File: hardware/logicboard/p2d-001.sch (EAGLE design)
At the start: 55 parts, among them IC1 74LS06N, IC2 4066N, J1 MKR, J2 GPIO, J3 Vcc, J4 RLY, J5 SPI, J7 DIN5, J8 DIN5, J9 DIN5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

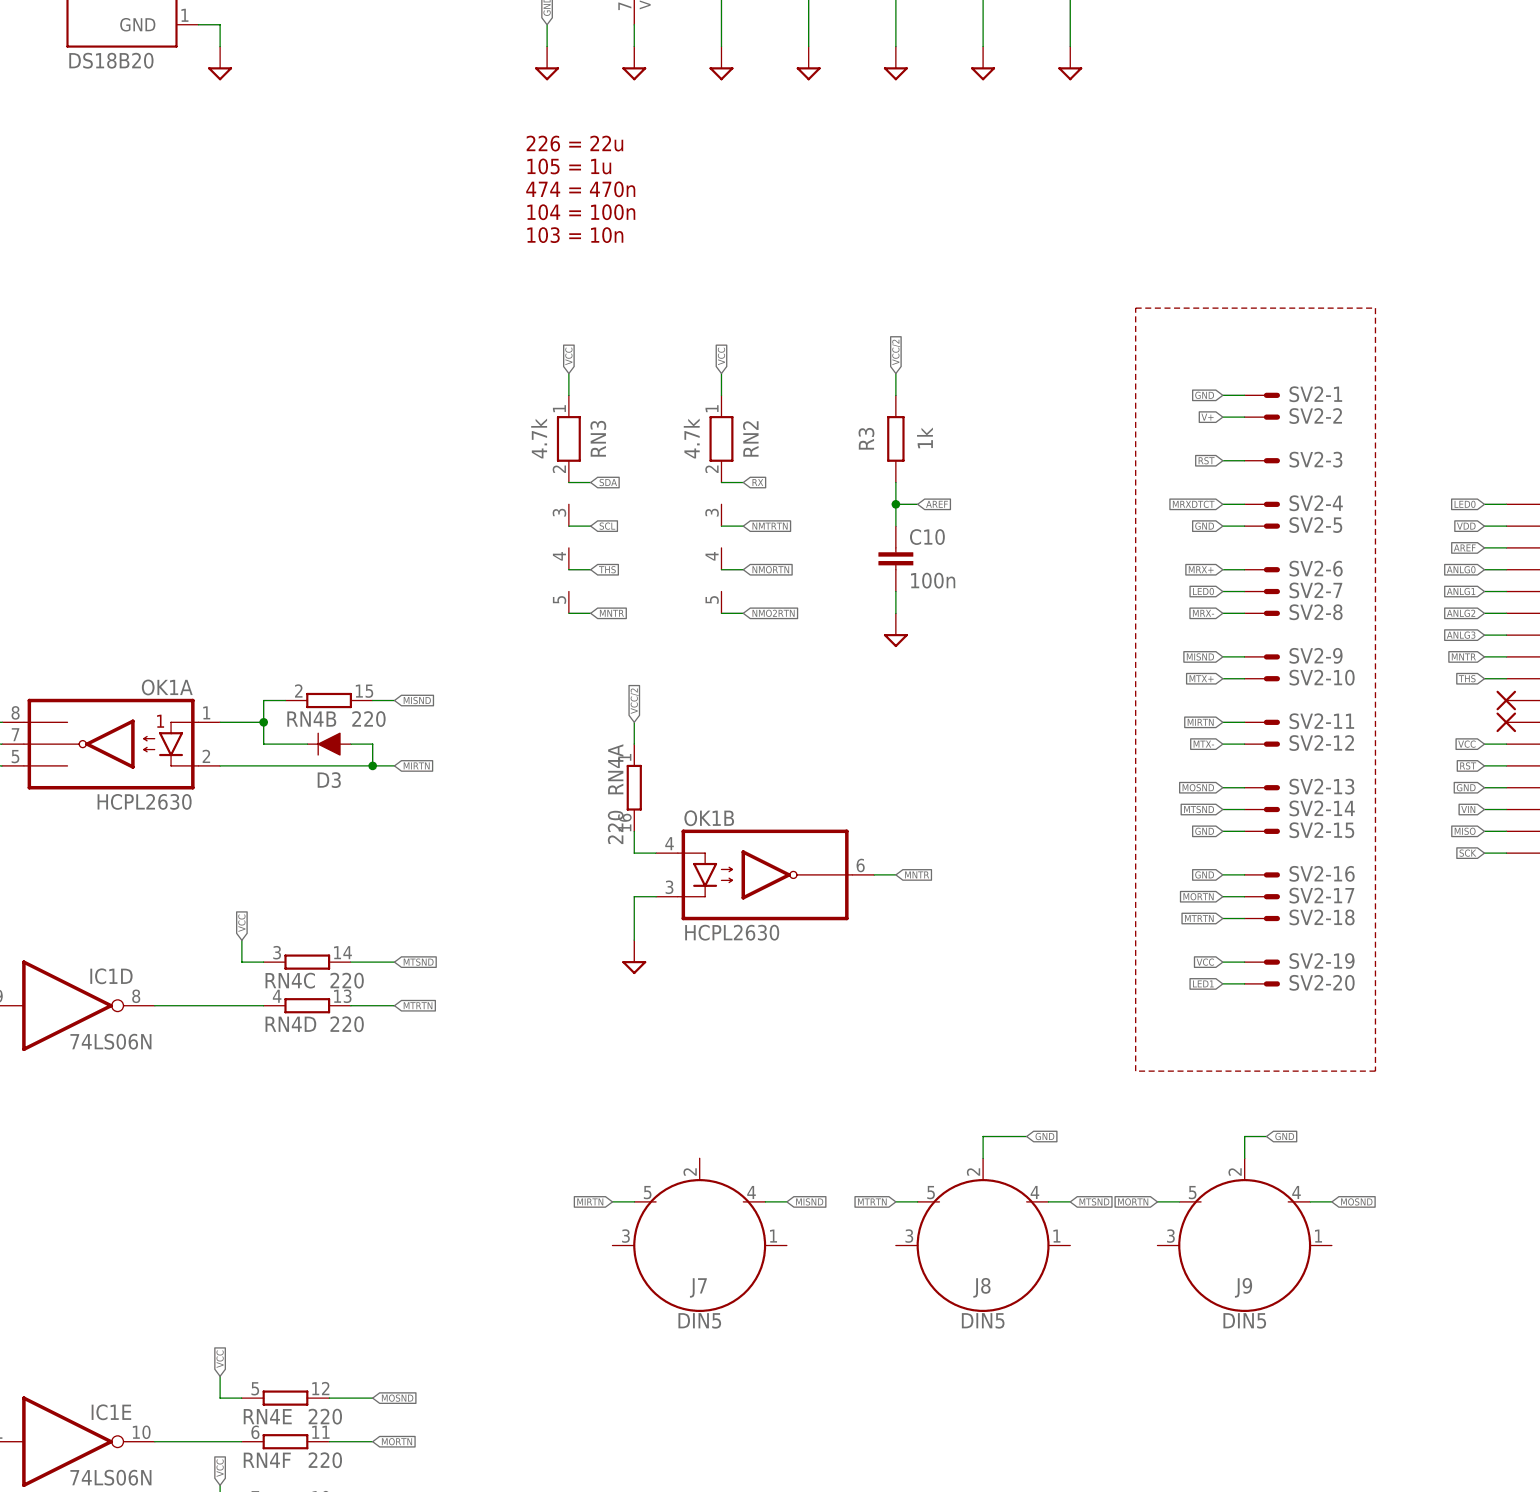
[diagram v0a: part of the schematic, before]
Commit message: Changed dimension of the board.
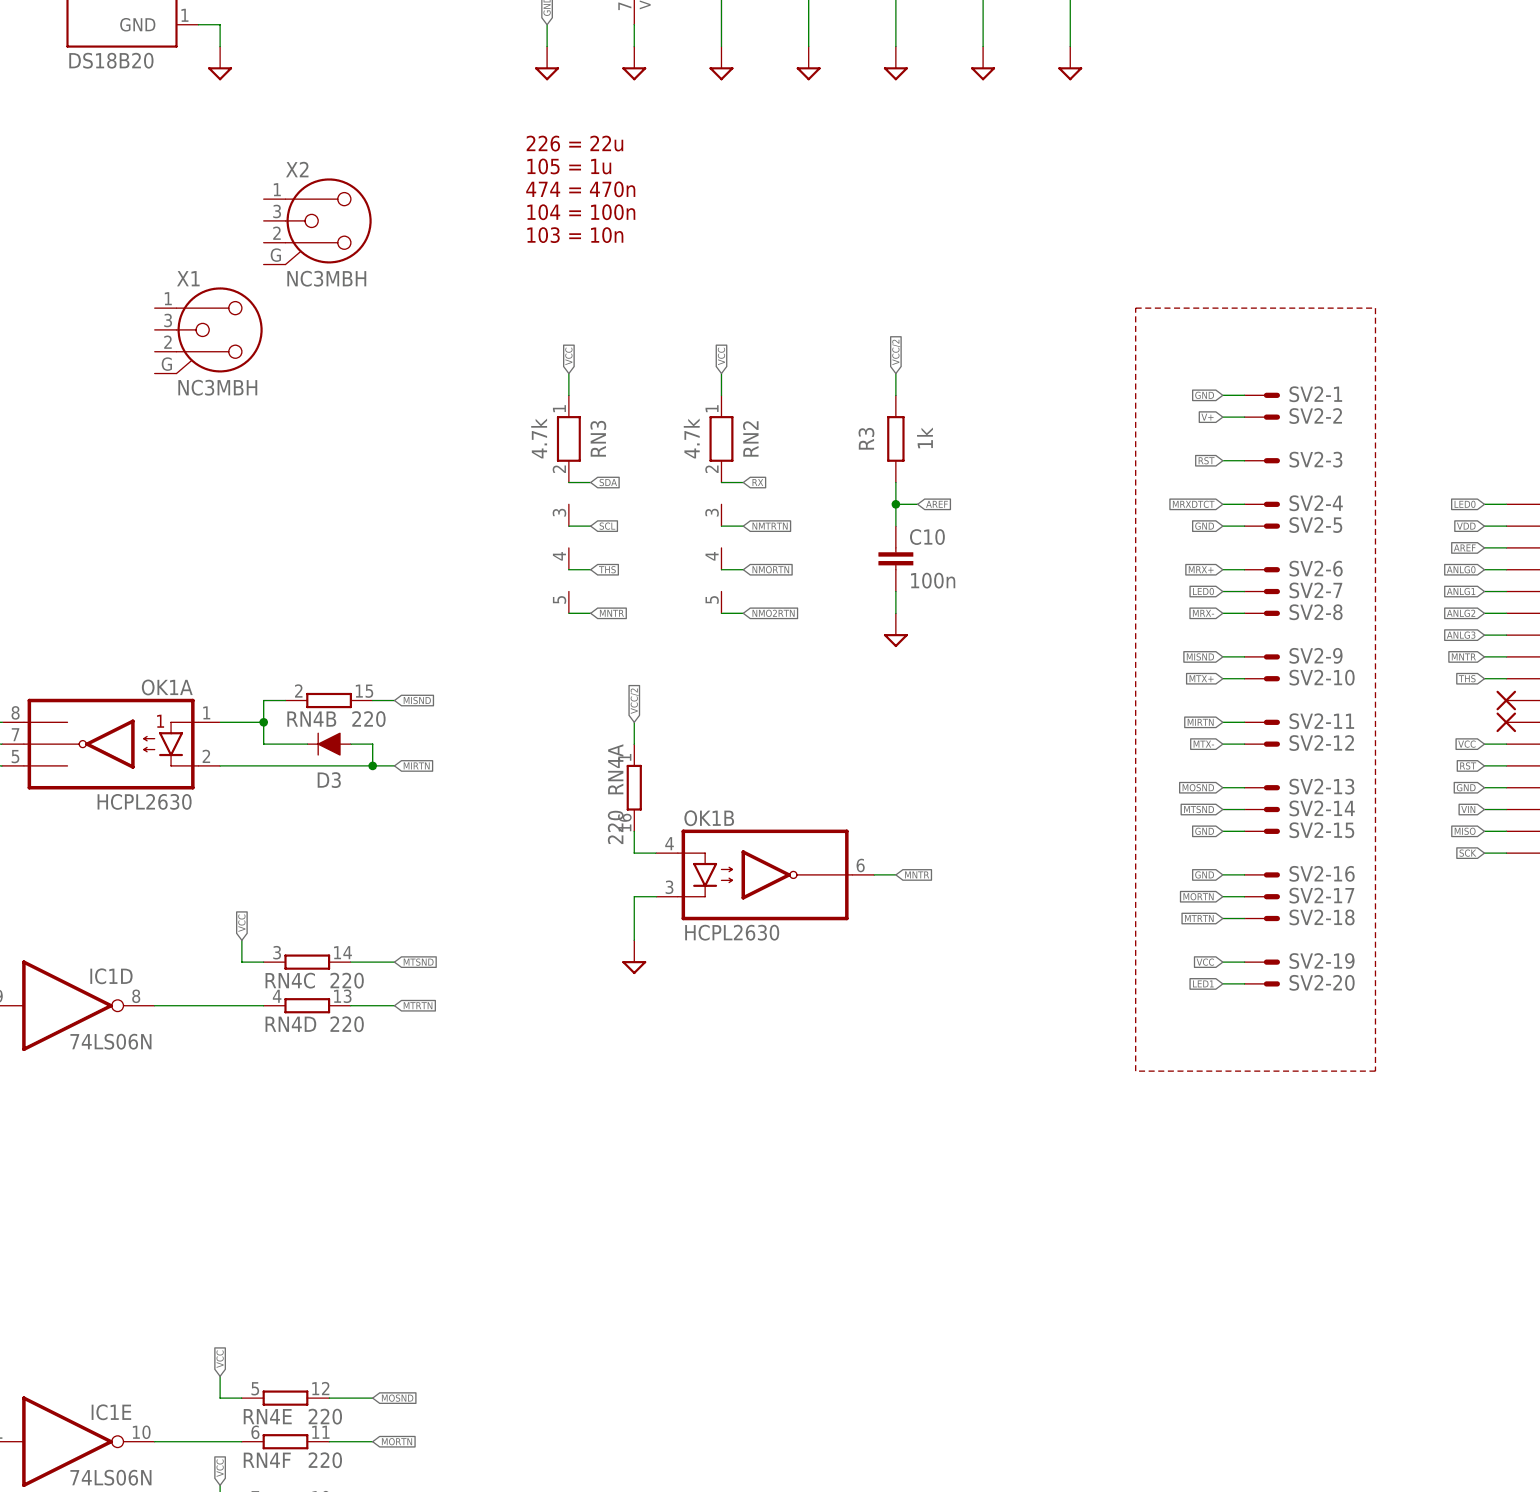
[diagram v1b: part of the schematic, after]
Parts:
- removed J7, J8, J9: DIN5, SparkFun-Connectors:DIN5
- added X1, X2: NC3MBH, con-neutrik_ag:NC3MBH
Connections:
- net GND: no longer J8.2, J9.2
- net MIRTN: no longer J7.5
- net MISND: no longer J7.4
- net MORTN: no longer J9.5
- net MOSND: no longer J9.4
- net MTRTN: no longer J8.5
- net MTSND: no longer J8.4
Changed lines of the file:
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@@
 <part name="V+" library="wirepad" library_urn="urn:adsk.eagle:library:412" deviceset="SMD2" device="" package3d_urn="urn:adsk.eagle:package:30839/1"/>
 <part name="VIN" library="wirepad" library_urn="urn:adsk.eagle:library:412" deviceset="SMD2" device="" package3d_urn="urn:adsk.eagle:package:30839/1"/>
-<part name="J7" library="SparkFun-Connectors" library_urn="urn:adsk.eagle:library:513" deviceset="DIN5" device="" package3d_urn="urn:adsk.eagle:package:38294/1"/>
-<part name="J8" library="SparkFun-Connectors" library_urn="urn:adsk.eagle:library:513" deviceset="DIN5" device="" package3d_urn="urn:adsk.eagle:package:38294/1"/>
-<part name="J9" library="SparkFun-Connectors" library_urn="urn:adsk.eagle:library:513" deviceset="DIN5" device="" package3d_urn="urn:adsk.eagle:package:38294/1"/>
 <part name="J0" library="con-jack" library_urn="urn:adsk.eagle:library:154" deviceset="JACK-PLUG" device="0" package3d_urn="urn:adsk.eagle:package:7492/1"/>
 <part name="R4" library="resistor" library_urn="urn:adsk.eagle:library:348" deviceset="R-EU_" device="0204/5" package3d_urn="urn:adsk.eagle:package:23488/1" value="1k"/>
@@
 <part name="SV3" library="con-ml" library_urn="urn:adsk.eagle:library:164" deviceset="ML14E" device="" package3d_urn="urn:adsk.eagle:package:8693/1"/>
 <part name="J6" library="SparkFun-Connectors" library_urn="urn:adsk.eagle:library:513" deviceset="CONN_03" device="JST-PTH-VERT" package3d_urn="urn:adsk.eagle:package:38080/1"/>
+<part name="X1" library="con-neutrik_ag" library_urn="urn:adsk.eagle:library:166" deviceset="NC3" device="MBH" package3d_urn="urn:adsk.eagle:package:8841/1"/>
+<part name="X2" library="con-neutrik_ag" library_urn="urn:adsk.eagle:library:166" deviceset="NC3" device="MBH" package3d_urn="urn:adsk.eagle:package:8841/1"/>
 </parts>
 <sheets>
@@
 <attribute name="VALUE" x="90.678" y="242.443" size="1.778" layer="96" rot="R270"/>
 </instance>
-<instance part="J7" gate="G$1" x="248.92" y="60.96" smashed="yes">
-<attribute name="NAME" x="248.92" y="55.372" size="1.778" layer="95" font="vector" align="bottom-center"/>
-<attribute name="VALUE" x="248.92" y="53.086" size="1.778" layer="96" font="vector" align="top-center"/>
-</instance>
-<instance part="J8" gate="G$1" x="281.94" y="60.96" smashed="yes">
-<attribute name="NAME" x="281.94" y="55.372" size="1.778" layer="95" font="vector" align="bottom-center"/>
-<attribute name="VALUE" x="281.94" y="53.086" size="1.778" layer="96" font="vector" align="top-center"/>
-</instance>
-<instance part="J9" gate="G$1" x="312.42" y="60.96" smashed="yes">
-<attribute name="NAME" x="312.42" y="55.372" size="1.778" layer="95" font="vector" align="bottom-center"/>
-<attribute name="VALUE" x="312.42" y="53.086" size="1.778" layer="96" font="vector" align="top-center"/>
-</instance>
 <instance part="J0" gate="G$1" x="33.02" y="198.12" smashed="yes">
 <attribute name="NAME" x="25.4" y="203.2" size="1.778" layer="95"/>
@@
 <attribute name="VALUE" x="63.5" y="12.954" size="1.778" layer="96" font="vector"/>
 <attribute name="NAME" x="63.5" y="25.908" size="1.778" layer="95" font="vector"/>
+</instance>
+<instance part="X1" gate="G$1" x="193.04" y="167.64" smashed="yes">
+<attribute name="NAME" x="187.96" y="172.72" size="1.778" layer="95"/>
+<attribute name="VALUE" x="187.96" y="160.02" size="1.778" layer="96"/>
+</instance>
+<instance part="X2" gate="G$1" x="205.74" y="180.34" smashed="yes">
+<attribute name="NAME" x="200.66" y="185.42" size="1.778" layer="95"/>
+<attribute name="VALUE" x="200.66" y="172.72" size="1.778" layer="96"/>
 </instance>
 </instances>
@@
 </segment>
 <segment>
-<pinref part="J8" gate="G$1" pin="2"/>
-<wire x1="281.94" y1="71.12" x2="281.94" y2="73.66" width="0.1524" layer="91"/>
-<wire x1="281.94" y1="73.66" x2="287.02" y2="73.66" width="0.1524" layer="91"/>
-<label x="287.02" y="73.66" size="0.8128" layer="95" xref="yes"/>
-</segment>
-<segment>
-<pinref part="J9" gate="G$1" pin="2"/>
-<wire x1="312.42" y1="71.12" x2="312.42" y2="73.66" width="0.1524" layer="91"/>
-<wire x1="312.42" y1="73.66" x2="314.96" y2="73.66" width="0.1524" layer="91"/>
-<label x="314.96" y="73.66" size="0.8128" layer="95" xref="yes"/>
-</segment>
-<segment>
 <pinref part="SUPPLY2" gate="GND" pin="GND"/>
 <wire x1="271.78" y1="208.28" x2="271.78" y2="200.66" width="0.1524" layer="91"/>
@@
 </segment>
 <segment>
-<pinref part="J7" gate="G$1" pin="4"/>
-<wire x1="256.54" y1="66.04" x2="259.08" y2="66.04" width="0.1524" layer="91"/>
-<label x="259.08" y="66.04" size="0.8128" layer="95" xref="yes"/>
-</segment>
-<segment>
 <pinref part="SV2" gate="-9" pin="S"/>
 <wire x1="312.42" y1="129.54" x2="309.88" y2="129.54" width="0.1524" layer="91"/>
@@
 </segment>
 <segment>
-<pinref part="J7" gate="G$1" pin="5"/>
-<wire x1="241.3" y1="66.04" x2="238.76" y2="66.04" width="0.1524" layer="91"/>
-<label x="238.76" y="66.04" size="0.8128" layer="95" rot="R180" xref="yes"/>
-</segment>
-<segment>
 <pinref part="SV2" gate="-11" pin="S"/>
 <wire x1="312.42" y1="121.92" x2="309.88" y2="121.92" width="0.1524" layer="91"/>
@@
 </segment>
 <segment>
-<pinref part="J9" gate="G$1" pin="5"/>
-<wire x1="304.8" y1="66.04" x2="302.26" y2="66.04" width="0.1524" layer="91"/>
-<label x="302.26" y="66.04" size="0.8128" layer="95" rot="R180" xref="yes"/>
-</segment>
-<segment>
 <pinref part="SV2" gate="-17" pin="S"/>
 <wire x1="312.42" y1="101.6" x2="309.88" y2="101.6" width="0.1524" layer="91"/>
@@
 <wire x1="210.82" y1="43.18" x2="205.74" y2="43.18" width="0.1524" layer="91"/>
 <pinref part="RN4" gate="E" pin="2"/>
-</segment>
-<segment>
-<pinref part="J9" gate="G$1" pin="4"/>
-<wire x1="320.04" y1="66.04" x2="322.58" y2="66.04" width="0.1524" layer="91"/>
-<label x="322.58" y="66.04" size="0.8128" layer="95" xref="yes"/>
 </segment>
 <segment>
@@
 </segment>
 <segment>
-<pinref part="J8" gate="G$1" pin="4"/>
-<wire x1="289.56" y1="66.04" x2="292.1" y2="66.04" width="0.1524" layer="91"/>
-<label x="292.1" y="66.04" size="0.8128" layer="95" xref="yes"/>
-</segment>
-<segment>
 <pinref part="SV2" gate="-14" pin="S"/>
 <wire x1="312.42" y1="111.76" x2="309.88" y2="111.76" width="0.1524" layer="91"/>
@@
 </segment>
 <segment>
-<pinref part="J8" gate="G$1" pin="5"/>
-<wire x1="274.32" y1="66.04" x2="271.78" y2="66.04" width="0.1524" layer="91"/>
-<label x="271.78" y="66.04" size="0.8128" layer="95" rot="R180" xref="yes"/>
-</segment>
-<segment>
